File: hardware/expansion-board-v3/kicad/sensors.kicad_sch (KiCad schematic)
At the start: 30 parts, among them J2 U.FL_GNSS_EXT(经尾线转SMA), J8 U.FL→内置patch, Q4 AO3401A, Q5 AO3401A, U17 XA17-G4K(或AS179-92LF), U4 BNO085, U5 BMP388, U6 QMC5883P, U7 ATGM336H-6N-74

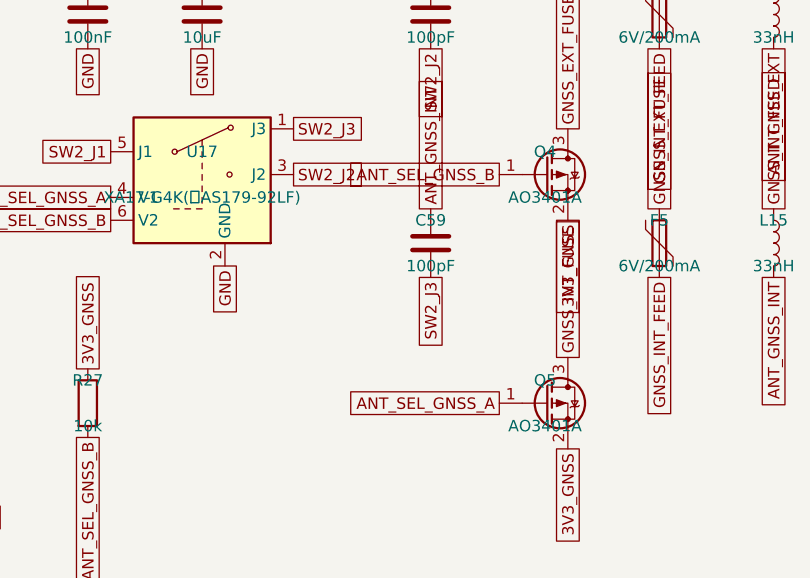
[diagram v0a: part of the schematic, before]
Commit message: fix(v3): correct GNSS antenna bias control
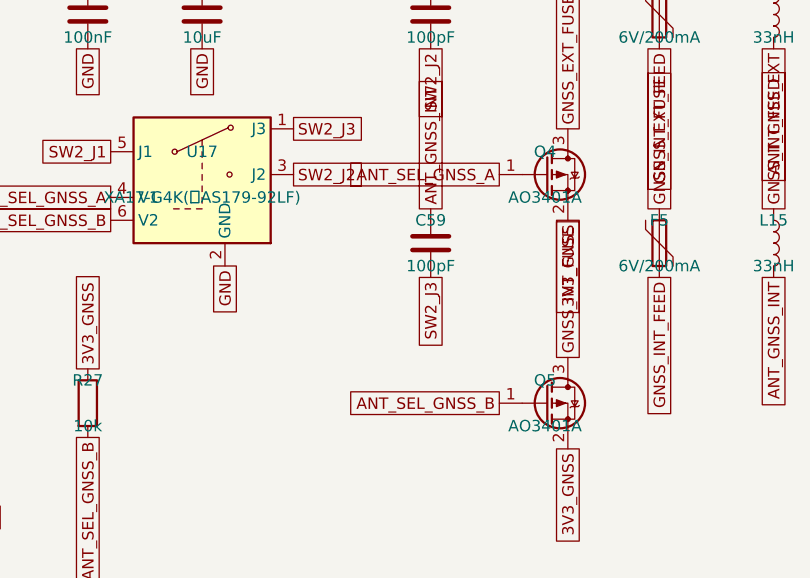
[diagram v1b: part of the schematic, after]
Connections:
- net ANT_SEL_GNSS_A: now also Q4.1 (G); no longer Q5.1 (G)
- net ANT_SEL_GNSS_B: now also Q5.1 (G); no longer Q4.1 (G)
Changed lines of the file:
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@@
 		)
 	)
-	(global_label "ANT_SEL_GNSS_B"
+	(global_label "ANT_SEL_GNSS_A"
 		(shape passive)
 		(at 274.32 88.9 180)
@@
 		)
 	)
-	(global_label "ANT_SEL_GNSS_A"
+	(global_label "ANT_SEL_GNSS_B"
 		(shape passive)
 		(at 274.32 114.3 180)

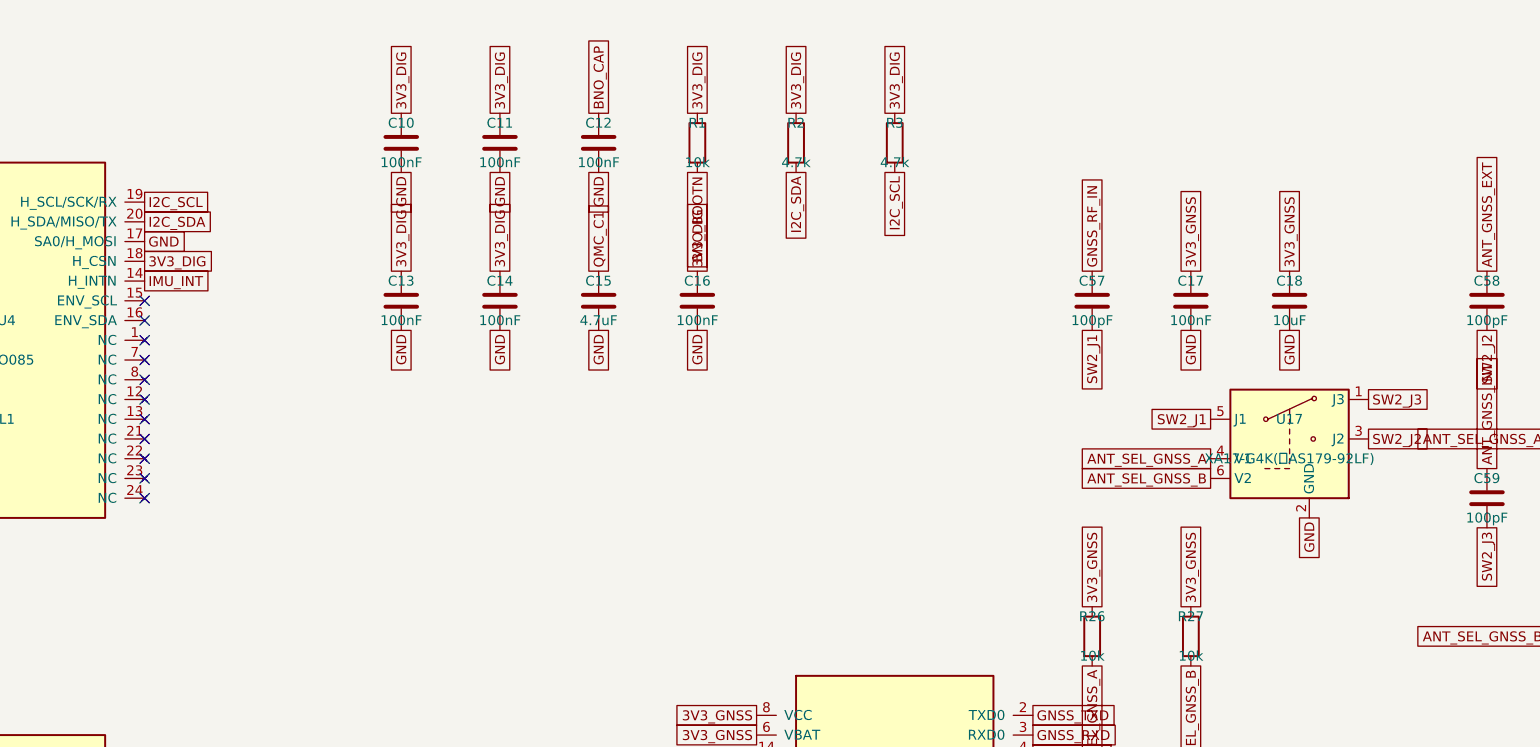
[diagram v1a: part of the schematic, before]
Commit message: feat(v3): backport V4 fixes into a clean V3.9 candidate (phases A-D)
Builds the V3.9 candidate from the V3.8 master rather than from the
working-tree intermediate. The intermediate had the 14 audit parts and a
cleared back side, but had lost 24 board-level silkscreen strings and all
four named RF zones - tools/rebuild.sh starts with gen_pcb.py, which calls
pcbnew.NewBoard(), and neither gr_text nor named zones live in
PLACEMENT.py or ROUTES.json, so every run drops them. The master is the
opposite: intact silkscreen and zones, missing only components. Adding
components back is enumerable (14 designators); restoring 24 silkscreen
strings with correct position, layer, size and mirroring is not.

Coordinates are transplanted from the intermediate, so nothing is
re-placed by hand. What that does cost is copper: the master was routed
without these parts, and 13 of the 18 land on existing tracks. Ripping
those out plus the resulting dangling chains removes 176 segments and 26
vias against the master's 1620/377 - all of it folded into phase E, which
was going to be manual routing anyway. Re-placing 13 parts on a fully
routed board would have been worse; C82-C86 are RP2040 local decouplers
that must stay next to the die, which is exactly how V4.3 ended up with
its 30 mm detour.

Phase B removes the AD8319 experimental branch (U13, R20, DET_TADJ). The
"directional error" turned out to reach into the generators, not just
prose - five places, of which two would have produced wrong hardware:

    gen_bom_smt.py   SKIP_REF = {"U14"}   the only detector excluded
                                          from the pick-and-place BOM
    gen_bom.py       ORDERED listed "AD8313ARMZ(备,二选一)", a suffixed
                     string that never matched the netlist value, so the
                     part had never once been classified

Ordering the V3.8 BOM as it stood would have produced a board whose 1090
receive chain has no detector at all. Phase B's hard criterion now holds:
excluding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
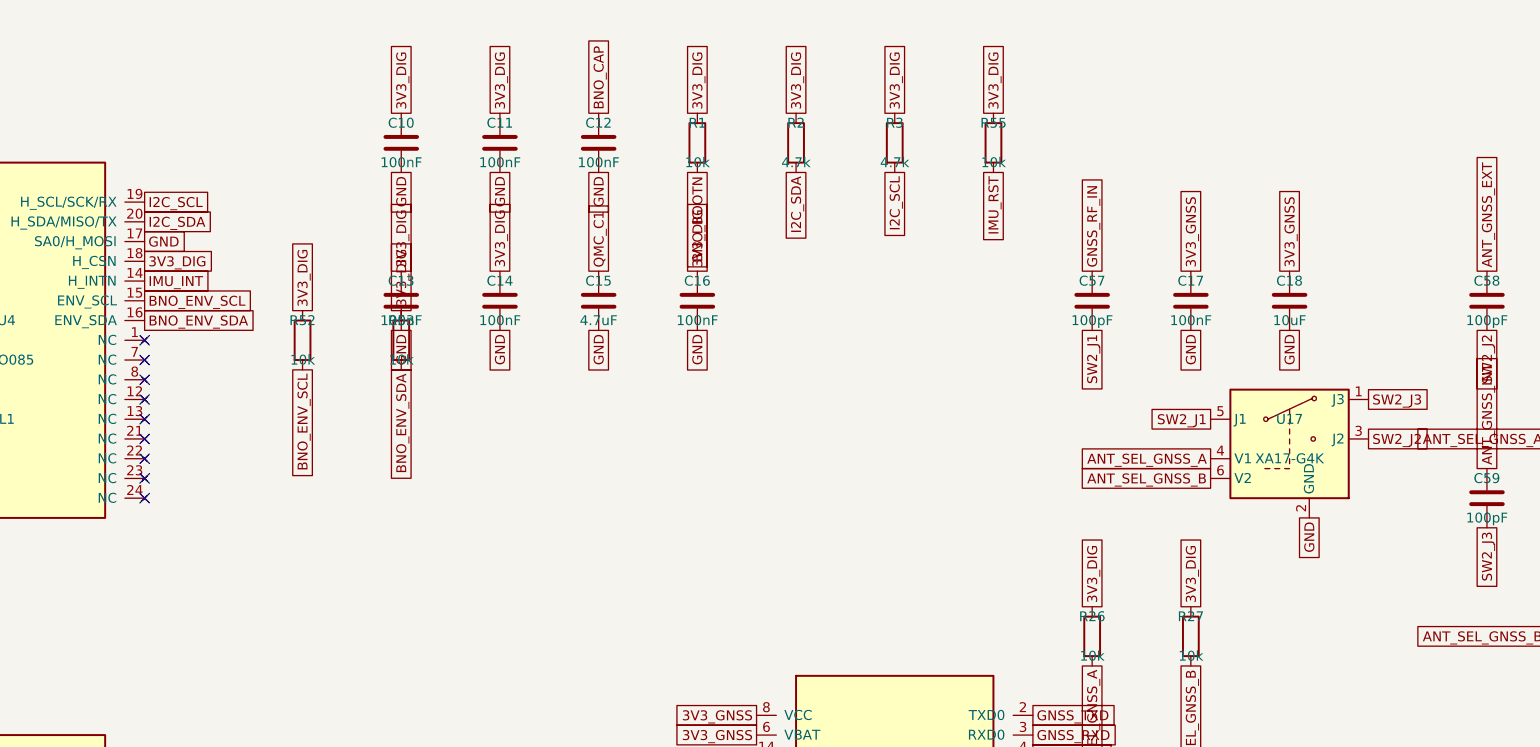
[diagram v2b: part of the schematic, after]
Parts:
- added R52, R53: 10k, Resistor_SMD:R_0402_1005Metric, symbol Device:R
- added R55: 10k, Resistor_SMD:R_0603_1608Metric, symbol Device:R
- U17: value XA17-G4K(或AS179-92LF) -> XA17-G4K
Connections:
- net 3V3_DIG: now also R26.1, R27.1, R52.1, R53.1, R55.1
- net 3V3_GNSS: no longer R26.1, R27.1
- net IMU_RST: now also R55.2
- net BNO_ENV_SCL: now reaches U4.15 (ENV_SCL)
- net BNO_ENV_SCL: now also R52.2
- net BNO_ENV_SDA: now reaches U4.16 (ENV_SDA)
- net BNO_ENV_SDA: now also R53.2
- no-connect marks 31 -> 29
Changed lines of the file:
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@@
 		(at 58.42 83.82)
 	)
+	(global_label "BNO_ENV_SCL"
+		(shape passive)
+		(at 93.98 71.12 0)
+		(effects (font (size 1.27 1.27)) (justify left))
+	)
+	(global_label "BNO_ENV_SDA"
+		(shape passive)
+		(at 93.98 73.66 0)
+		(effects (font (size 1.27 1.27)) (justify left))
+	)
 	(global_label "I2C_SCL"
 		(shape passive)
@@
 	)
 	(no_connect
-		(at 93.98 71.12)
-	)
-	(no_connect
-		(at 93.98 73.66)
-	)
-	(no_connect
 		(at 93.98 76.2)
 	)
@@
 	(no_connect
 		(at 93.98 96.52)
+	)
+	(symbol
+		(lib_id "Device:R")
+		(at 114.3 76.2 0)
+		(unit 1)
+		(exclude_from_sim no)
+		(in_bom yes)
+		(on_board yes)
+		(dnp no)
+		(property "Reference" "R52"
+			(at 114.3 73.66 0)
+			(effects (font (size 1.27 1.27)))
+		)
+		(property "Value" "10k"
+			(at 114.3 78.74 0)
+			(effects (font (size 1.27 1.27)))
+		)
+		(property "Footprint" "Resistor_SMD:R_0402_1005Metric"
+			(at 114.3 81.28 0)
+			(effects (font (size 1.27 1.27))
+				(hide yes))
+		)
+		(property "Datasheet" "~"
+			(at 114.3 83.82 0)
+			(effects (font (size 1.27 1.27))
+				(hide yes))
+		)
+		(pin "1"
+		)
+		(pin "2"
+		)
+		(instances
+			(project "expansion-board-v3"
+				(path "/10000000-0000-4000-8000-000000000001/20000000-0000-4000-8000-000000000005"
+					(reference "R52")
+					(unit 1)
+				)
+			)
+		)
+	)
+	(global_label "3V3_DIG"
+		(shape passive)
+		(at 114.3 72.39 270)
+		(effects (font (size 1.27 1.27)) (justify left))
+	)
+	(global_label "BNO_ENV_SCL"
+		(shape passive)
+		(at 114.3 80.01 90)
+		(effects (font (size 1.27 1.27)) (justify right))
+	)
+	(symbol
+		(lib_id "Device:R")
+		(at 127 76.2 0)
+		(unit 1)
+		(exclude_from_sim no)
+		(in_bom yes)
+		(on_board yes)
+		(dnp no)
+		(property "Reference" "R53"
+			(at 127 73.66 0)
+			(effects (font (size 1.27 1.27)))
+		)
+		(property "Value" "10k"
+			(at 127 78.74 0)
+			(effects (font (size 1.27 1.27)))
+		)
+		(property "Footprint" "Resistor_SMD:R_0402_1005Metric"
+			(at 127 81.28 0)
+			(effects (font (size 1.27 1.27))
+				(hide yes))
+		)
+		(property "Datasheet" "~"
+			(at 127 83.82 0)
+			(effects (font (size 1.27 1.27))
+				(hide yes))
+		)
+		(pin "1"
+		)
+		(pin "2"
+		)
+		(instances
+			(project "expansion-board-v3"
+				(path "/10000000-0000-4000-8000-000000000001/20000000-0000-4000-8000-000000000005"
+					(reference "R53")
+					(unit 1)
+				)
+			)
+		)
+	)
+	(global_label "3V3_DIG"
+		(shape passive)
+		(at 127 72.39 270)
+		(effects (font (size 1.27 1.27)) (justify left))
+	)
+	(global_label "BNO_ENV_SDA"
+		(shape passive)
+		(at 127 80.01 90)
+		(effects (font (size 1.27 1.27)) (justify right))
 	)
 	(symbol
@@
 			(effects (font (size 1.27 1.27)))
 		)
-		(property "Value" "XA17-G4K(或AS179-92LF)"
+		(property "Value" "XA17-G4K"
 			(at 241.3 91.44 0)
 			(effects (font (size 1.27 1.27)))
@@
 	(symbol
 		(lib_id "Device:R")
+		(at 203.2 50.8 0)
+		(unit 1)
+		(exclude_from_sim no)
+		(in_bom yes)
+		(on_board yes)
+		(dnp no)
+		(property "Reference" "R55"
+			(at 203.2 48.26 0)
+			(effects (font (size 1.27 1.27)))
+		)
+		(property "Value" "10k"
+			(at 203.2 53.34 0)
+			(effects (font (size 1.27 1.27)))
+		)
+		(property "Footprint" "Resistor_SMD:R_0603_1608Metric"
+			(at 203.2 55.88 0)
+			(effects (font (size 1.27 1.27))
+				(hide yes))
+		)
+		(property "Datasheet" "~"
+			(at 203.2 58.42 0)
+			(effects (font (size 1.27 1.27))
+				(hide yes))
+		)
+		(pin "1"
+		)
+		(pin "2"
+		)
+		(instances
+			(project "expansion-board-v3"
+				(path "/10000000-0000-4000-8000-000000000001/20000000-0000-4000-8000-000000000005"
+					(reference "R55")
+					(unit 1)
+				)
+			)
+		)
+	)
+	(global_label "3V3_DIG"
+		(shape passive)
+		(at 203.2 46.99 270)
+		(effects (font (size 1.27 1.27)) (justify left))
+	)
+	(global_label "IMU_RST"
+		(shape passive)
+		(at 203.2 54.61 90)
+		(effects (font (size 1.27 1.27)) (justify right))
+	)
+	(symbol
+		(lib_id "Device:R")
 		(at 215.9 114.3 0)
 		(unit 1)
@@
 		)
 	)
-	(global_label "3V3_GNSS"
+	(global_label "3V3_DIG"
 		(shape passive)
 		(at 215.9 110.49 270)
@@
 		)
 	)
-	(global_label "3V3_GNSS"
+	(global_label "3V3_DIG"
 		(shape passive)
 		(at 228.6 110.49 270)

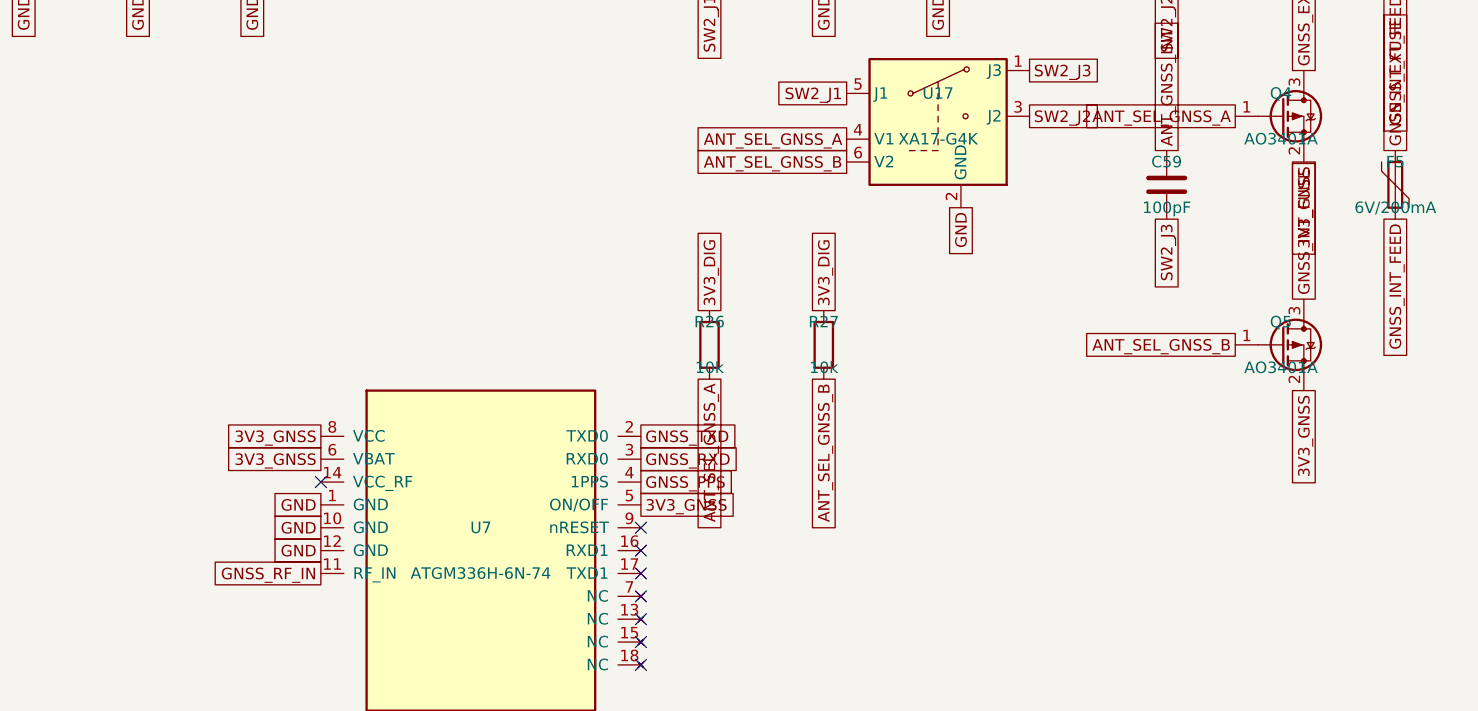
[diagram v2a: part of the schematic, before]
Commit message: hardware: v4 走线固化 + V4.5 发布包 + 装配站点/子项目
- v3/v4 kicad_pcb 重新布线; export_routes 快照 ROUTES.json(1609 段/438 孔)。
- V4.5 Gerber/KiCad 发布包(20260911); cal-board/fpc-antenna 子项目;
  web/assembly 装配站点与生成工具; V4.6 airband BOM 草案。
- 文档: BASEBOARD_REF / ASSEMBLY / SELECTIVE_PLACEMENT 等同步。
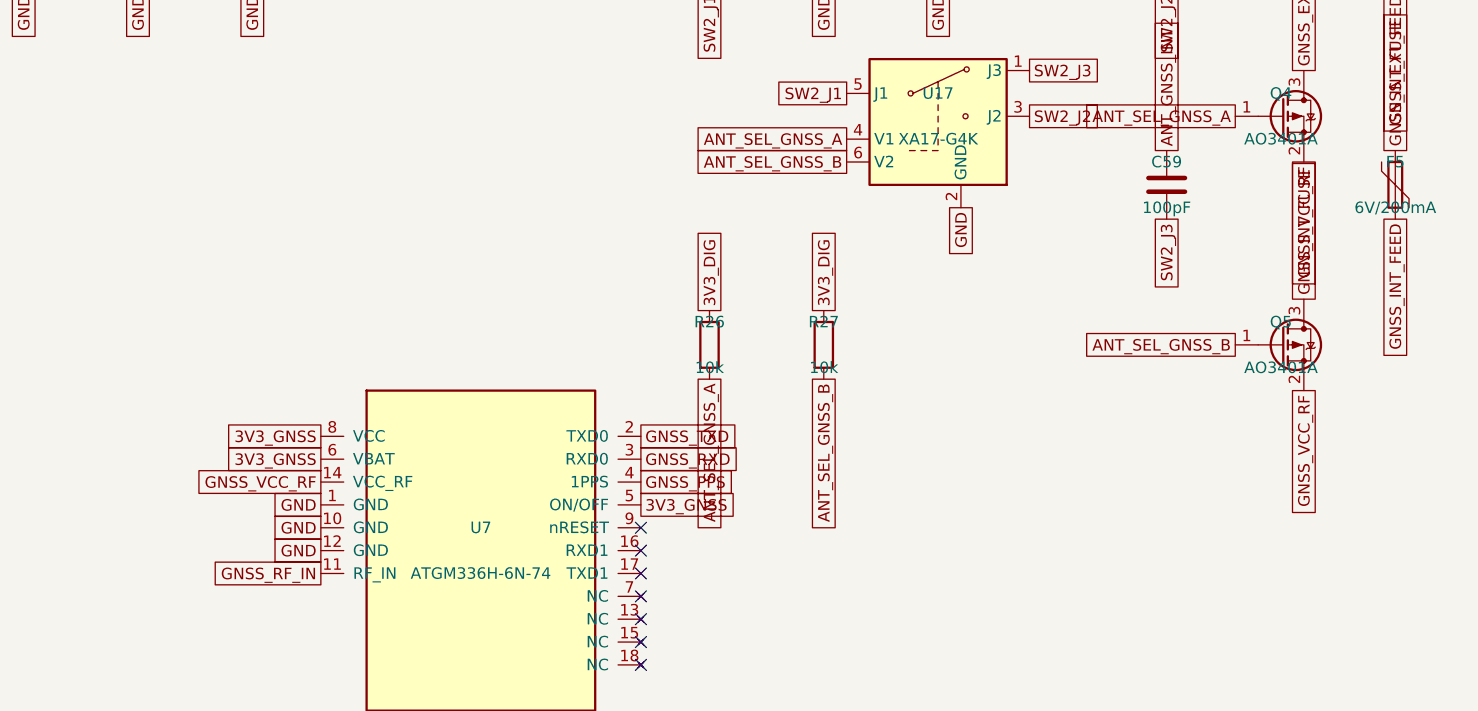
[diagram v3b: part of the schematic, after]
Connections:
- net 3V3_GNSS: no longer Q4.2 (S), Q5.2 (S)
- net GNSS_VCC_RF: now reaches U7.14 (VCC_RF)
- net GNSS_VCC_RF: now also Q4.2 (S), Q5.2 (S)
- no-connect marks 29 -> 28
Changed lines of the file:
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@@
 		(effects (font (size 1.27 1.27)) (justify right))
 	)
-	(no_connect
-		(at 172.72 129.54)
+	(global_label "GNSS_VCC_RF"
+		(shape passive)
+		(at 172.72 129.54 180)
+		(effects (font (size 1.27 1.27)) (justify right))
 	)
 	(global_label "GNSS_RF_IN"
@@
 		(effects (font (size 1.27 1.27)) (justify right))
 	)
-	(global_label "3V3_GNSS"
+	(global_label "GNSS_VCC_RF"
 		(shape passive)
 		(at 281.94 93.98 90)
@@
 		(effects (font (size 1.27 1.27)) (justify right))
 	)
-	(global_label "3V3_GNSS"
+	(global_label "GNSS_VCC_RF"
 		(shape passive)
 		(at 281.94 119.38 90)
